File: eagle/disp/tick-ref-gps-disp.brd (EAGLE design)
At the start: 127 x 133.3 mm, 37 parts, among them CN1 To Main Board, Q1 MMBT3904, U1 AS1115, U2 AS1115

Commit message: Routing continues, 9 airwires to go.
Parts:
- added LED10, LED11, LED12, LED13, LED14, LED15, LED16, LED17, LED18, LED19, LED20, LED21, LED22, LED7, LED8, LED9: (no value), led:CHIP-LED0805
- moved DSP5 4.76 mm to (20.4, 31.8)
- moved DSP6 4.76 mm to (27.4, 31.8)
- moved DSP11 4.76 mm to (85.2, 31.8)
- moved DSP12 4.76 mm to (92.1, 31.8)
- moved DSP10 1.59 mm to (70.5, 31.8)
- moved DSP7 1.59 mm to (42.0, 31.8)
- moved DSP8 1.59 mm to (49.0, 31.8)
- moved DSP9 1.59 mm to (63.6, 31.8)
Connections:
- net N$1 renamed 1PPS_R_Q
- removed net CATH_SATS_MS: DSP4.3, DSP4.8, U2.9
- new net CATH_STATUS_MS: DSP4.3, DSP4.8, LED21.C, U2.9
- new net CATH_STRENGTH: LED22.C, U2.10
- new net DSPA_SEG_DP: LED15.A, LED16.A, LED17.A, LED18.A, LED19.A, LED20.A, LED21.A, LED22.A, U2.22
- new net DSPB_SEG_DP: LED10.C, LED11.C, LED12.C, LED13.C, LED14.C, LED7.C, LED8.C, LED9.C, U1.22
- net CATH_HOUR_LS: now also LED16.C
- net CATH_HOUR_MS: now also LED15.C
- net CATH_MIN_LS: now also LED18.C
- net CATH_MIN_MS: now also LED17.C
- net CATH_SEC_LS: now also LED20.C
- net CATH_SEC_MS: now also LED19.C
- net DSP10-C: now also LED12.A
- net DSP11-C: now also LED13.A
- net DSP12-C: now also LED14.A
- net DSP5-C: now also LED7.A
- net DSP6-C: now also LED8.A
- net DSP7-C: now also LED9.A
- net DSP8-C: now also LED10.A
- net DSP9-C: now also LED11.A
- net DSPB_SEG_G: now also U1.11
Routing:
- net DSPB_SEG_DP: track 0.00 -> 124.8 mm, vias 0 -> 8
- net DSPA_SEG_DP: track 0.00 -> 78.3 mm, vias 0 -> 13
- net +5V: track 241.8 -> 299.6 mm
- net CATH_MIN_LS: track 55.7 -> 112.9 mm, vias 4 -> 8
- net CATH_HOUR_LS: track 51.3 -> 105.5 mm, vias 2 -> 6
- net CATH_MIN_MS: track 53.1 -> 106.0 mm, vias 4 -> 8
- net CATH_HOUR_MS: track 52.4 -> 102.0 mm, vias 2 -> 4
- net DSP9-C: track 40.9 -> 75.7 mm, vias 4 -> 9
- net 1PPS: track 101.2 -> 133.2 mm
- net LED_COMM: track 93.1 -> 122.3 mm
- net LED_OK: track 84.0 -> 113.2 mm
- net LED_FAULT: track 65.8 -> 95.0 mm
- net LED_WAIT: track 75.1 -> 104.3 mm
- net DSPB_SEG_G: track 154.9 -> 125.7 mm, vias 2 -> 3
- net DSP10-C: track 34.9 -> 59.5 mm, vias 4 -> 7
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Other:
- outline, holes or cut-outs redrawn

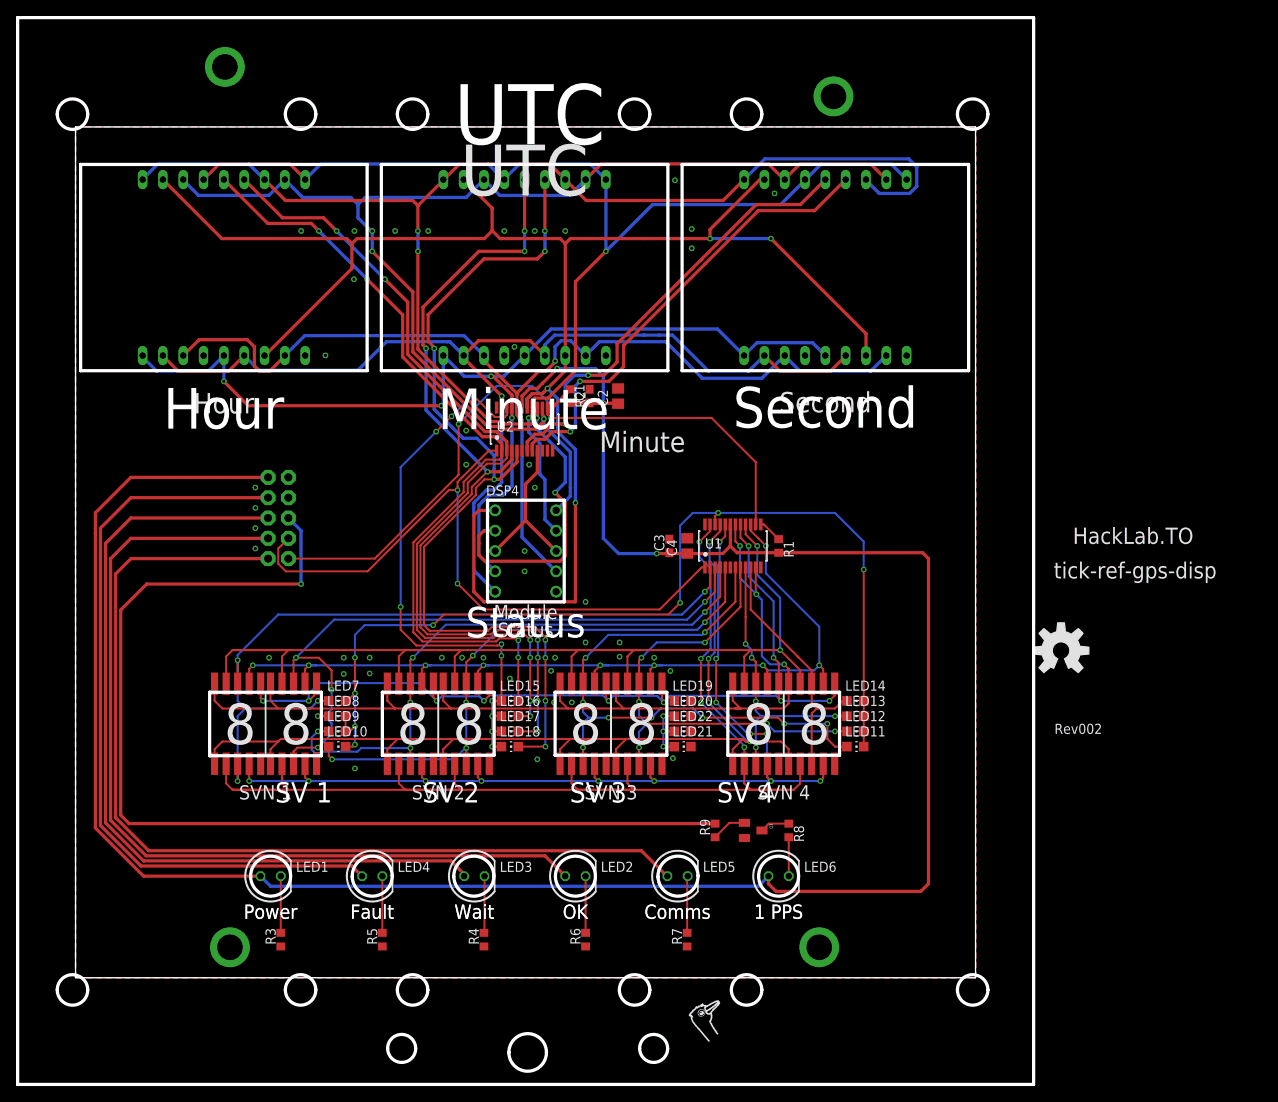
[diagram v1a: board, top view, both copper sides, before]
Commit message: Completed routing tick-ref-gps-disp board rev002.
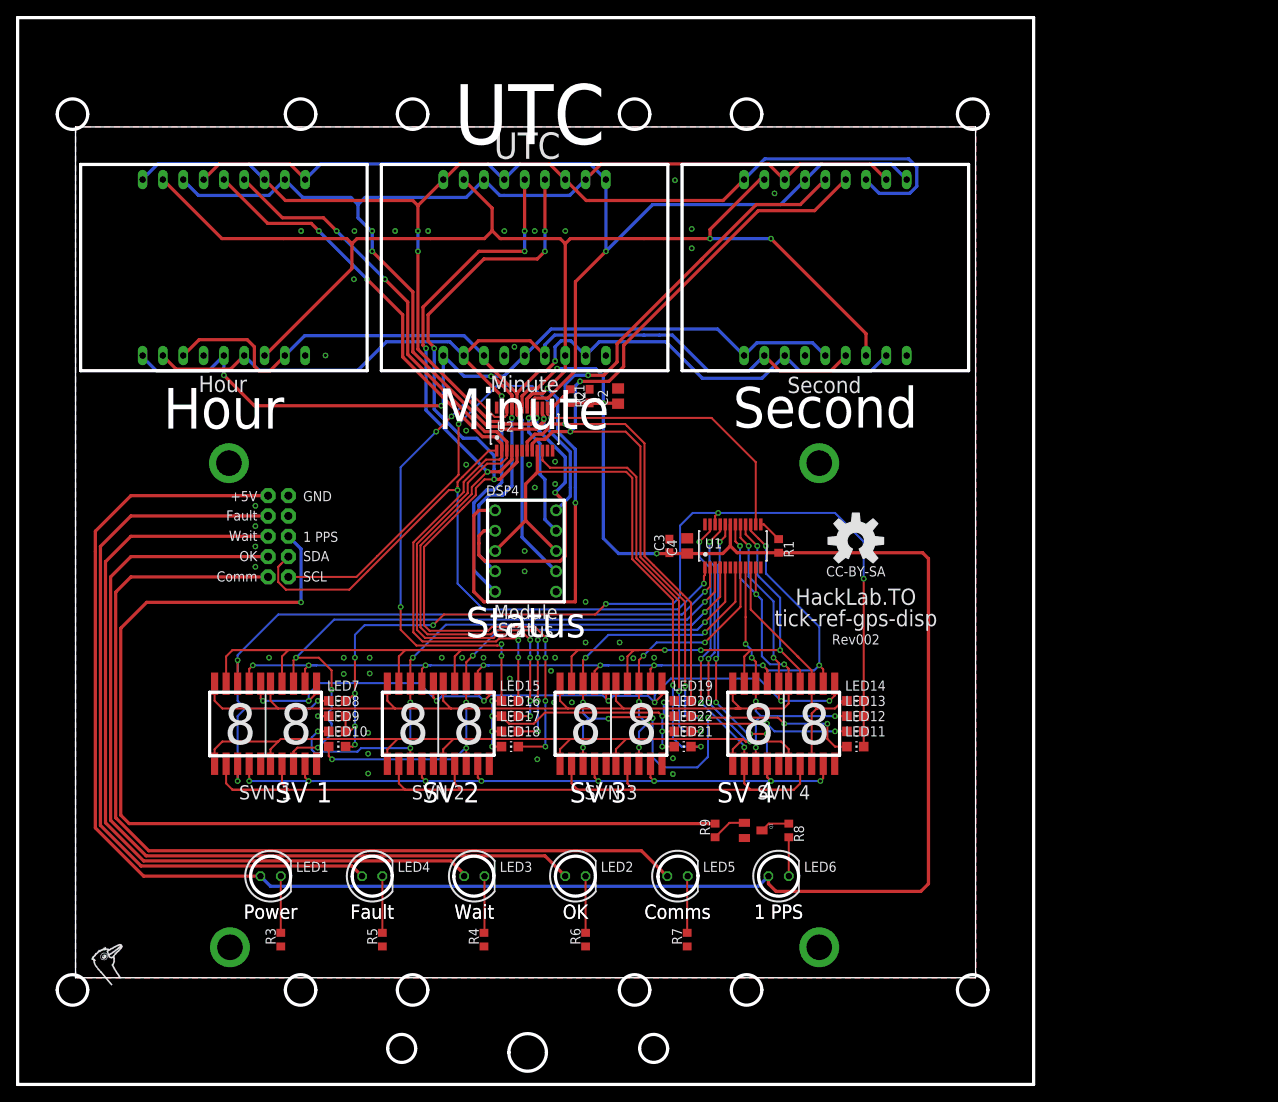
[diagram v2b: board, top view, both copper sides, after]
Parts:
- moved U$2 75.0 mm to (3.75, 1.08)
- moved U$1 29.1 mm to (97.5, 54.6)
- moved CN1 2.29 mm to (25.3, 55.2)
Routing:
- net CATH_STATUS_MS: track 20.1 -> 72.4 mm, vias 0 -> 2
- net CATH_STRENGTH: track 0.00 -> 51.4 mm, vias 0 -> 2
- net CATH_SEC_LS: track 58.2 -> 107.0 mm, vias 2 -> 4
- net CATH_SEC_MS: track 56.2 -> 101.7 mm
- net DSPA_SEG_DP: track 78.3 -> 103.2 mm, vias 13 -> 14
- net DSP9-C: track 75.7 -> 85.8 mm
- net DSPB_SEG_B: track 116.2 -> 118.9 mm
- net LED_OK: track 113.2 -> 110.9 mm
- net LED_FAULT: track 95.0 -> 92.7 mm
- net LED_COMM: track 122.3 -> 120.0 mm
- net 1PPS: track 133.2 -> 130.9 mm
- net +5V: track 299.6 -> 297.3 mm
- net LED_WAIT: track 104.3 -> 102.0 mm
- net SDA: track 84.4 -> 86.4 mm
- net SCL: track 85.3 -> 86.2 mm
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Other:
- board text added: "+5V"
- board text added: "CC-BY-SA"
- board text added: "Comm"
- board text added: "GND"
- board text added: "SCL"
- board text added: "SDA"
- board text added: "designed by sen, 2014"
- board text added: "http://hackstrich.sen.cx/HackLab.TO_Timing_Reference_A"
